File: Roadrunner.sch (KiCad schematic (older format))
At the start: 57 parts, among them J1 USB_OTG, J10 Digital, J11 ~WAKE, J13 SERIAL 4, J14 SERIAL 3, J15 -AREF, J16 +AREF, J17 SPI 2 (D22,D23), J19 SERIAL 2, J2 JTAG, J20 SPI 0, J21 SERIAL 1, J3 ~RST, J4 PF4, J5 ~HIB, J6 VIn, J7 Power, J8 Analog, J9 Digital, Q1 UM6K33N, Q2 UM6K33N, SW1 RESET, T1 M_Hole, T2 M_Hole, T3 M_Hole, T4 M_Hole, U1 TM4C123GH6PM, U2 LM1117-3.3, Y1 32.768Khz, Y2 16MHz

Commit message: Renaming project ro Roadrunner
Also include various routing changes and a new logo
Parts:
- C2: Description (none) -> 24pF ±5% 50V Ceramic Capacitor C0G, NP0 0603; Part # (none) -> CC0603JRNPO9BN240
- Q1, Q2: Part # (none) -> UM6K33NTN
- R1: Part # ERJ-3EKF1002V -> RC0603FR-0710KL
- R2: Part # ERJ-3EKF1004V -> RCG06031M00FKEA
- RN2: Part # YC164-JR-0710KL -> EXB-38V103JV
- U2: Part # (none) -> LM1117IMPX-3.3/NOPB
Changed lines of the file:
@@
 LIBS:tm4c123gh6pm
 LIBS:project_symbols
-LIBS:Arduino_Leo_Tiva-cache
+LIBS:Roadrunner-cache
 EELAYER 25 0
 EELAYER END
@@
 Title "Roadrunner (Arduino-Tiva)"
 Date "2017-07-22"
-Rev "v1.1"
+Rev "v1.1.2"
 Comp "Jacob Miller"
 Comment1 "TM4C123G"
@@
 F 1 "10k" V 1500 1050 50  0000 C CNN
 F 2 "Resistors_SMD:R_0603_HandSoldering" V 1430 1050 50  0001 C CNN
-F 3 "http://industrial.panasonic.com/www-cgi/jvcr13pz.cgi?E+PZ+3+AOA0002+ERJ3EKF1002V+7+WW" H 1500 1050 50  0001 C CNN
+F 3 "http://www.yageo.com/pdf/Pu-RC0603_51_PbFree_L_2.pdf" H 1500 1050 50  0001 C CNN
 F 4 "10k Ohm ±1% 0.1W, 1/10W Chip Resistor 0603 (1608 Metric) Automotive AEC-Q200 Thick Film" V 1500 1050 60  0001 C CNN "Description"
-F 5 "ERJ-3EKF1002V" V 1500 1050 60  0001 C CNN "Part #"
+F 5 "RC0603FR-0710KL" V 1500 1050 60  0001 C CNN "Part #"
 	1    1500 1050
 	1    0    0    -1
 $EndComp
 $Comp
-L +3.3V #PWR01
+L +3.3V #PWR6
 U 1 1 58E00512
 P 1500 800
-F 0 "#PWR01" H 1500 650 50  0001 C CNN
+F 0 "#PWR6" H 1500 650 50  0001 C CNN
 F 1 "+3.3V" H 1500 940 50  0000 C CNN
 F 2 "" H 1500 800 50  0001 C CNN
@@
 $EndComp
 $Comp
-L C_Small C2
-U 1 1 58E01071
-P 3450 4450
-F 0 "C2" H 3460 4520 50  0000 L CNN
-F 1 "24pF" H 3460 4370 50  0000 L CNN
-F 2 "Capacitors_SMD:C_0603" H 3450 4450 50  0001 C CNN
-F 3 "" H 3450 4450 50  0001 C CNN
-	1    3450 4450
-	0    -1   -1   0
-$EndComp
-$Comp
-L GNDREF #PWR02
+L GNDREF #PWR9
 U 1 1 58E01B5B
 P 3000 3700
-F 0 "#PWR02" H 3000 3450 50  0001 C CNN
+F 0 "#PWR9" H 3000 3450 50  0001 C CNN
 F 1 "GNDREF" H 3000 3550 50  0001 C CNN
 F 2 "" H 3000 3700 50  0001 C CNN
@@
 $EndComp
 $Comp
-L GNDREF #PWR03
+L GNDREF #PWR11
 U 1 1 58E01B81
 P 3500 3700
-F 0 "#PWR03" H 3500 3450 50  0001 C CNN
+F 0 "#PWR11" H 3500 3450 50  0001 C CNN
 F 1 "GNDREF" H 3500 3550 50  0001 C CNN
 F 2 "" H 3500 3700 50  0001 C CNN
@@
 $EndComp
 $Comp
-L GNDREF #PWR04
+L GNDREF #PWR2
 U 1 1 58E02126
 P 1000 1300
-F 0 "#PWR04" H 1000 1050 50  0001 C CNN
+F 0 "#PWR2" H 1000 1050 50  0001 C CNN
 F 1 "GNDREF" H 1000 1150 50  0001 C CNN
 F 2 "" H 1000 1300 50  0001 C CNN
@@
 $EndComp
 $Comp
-L GNDREF #PWR05
+L GNDREF #PWR1
 U 1 1 58E02513
 P 800 4950
-F 0 "#PWR05" H 800 4700 50  0001 C CNN
+F 0 "#PWR1" H 800 4700 50  0001 C CNN
 F 1 "GNDREF" H 800 4800 50  0001 C CNN
 F 2 "" H 800 4950 50  0001 C CNN
@@
 $EndComp
 $Comp
-L GNDREF #PWR06
+L GNDREF #PWR15
 U 1 1 58E0281C
 P 5550 5700
-F 0 "#PWR06" H 5550 5450 50  0001 C CNN
+F 0 "#PWR15" H 5550 5450 50  0001 C CNN
 F 1 "GNDREF" H 5550 5550 50  0001 C CNN
 F 2 "" H 5550 5700 50  0001 C CNN
@@
 $EndComp
 $Comp
-L +3.3V #PWR07
+L +3.3V #PWR16
 U 1 1 58E02E1C
 P 5650 900
-F 0 "#PWR07" H 5650 750 50  0001 C CNN
+F 0 "#PWR16" H 5650 750 50  0001 C CNN
 F 1 "+3.3V" H 5650 1040 50  0000 C CNN
 F 2 "" H 5650 900 50  0001 C CNN
@@
 F 1 "1M" V 1750 2000 50  0000 C CNN
 F 2 "Resistors_SMD:R_0603_HandSoldering" V 1680 2000 50  0001 C CNN
-F 3 "https://industrial.panasonic.com/cdbs/www-data/pdf/RDA0000/AOA0000C283.pdf" H 1750 2000 50  0001 C CNN
+F 3 "http://www.vishay.com/docs/20047/rcge3.pdf" H 1750 2000 50  0001 C CNN
 F 4 "1M Ohm ±1% 0.1W, 1/10W Chip Resistor 0603 (1608 Metric) Automotive AEC-Q200 Thick Film" V 1750 2000 60  0001 C CNN "Description"
-F 5 "ERJ-3EKF1004V" V 1750 2000 60  0001 C CNN "Part #"
+F 5 "RCG06031M00FKEA" V 1750 2000 60  0001 C CNN "Part #"
 	1    1750 2000
 	0    1    1    0
 $EndComp
 $Comp
-L +3.3V #PWR08
+L +3.3V #PWR8
 U 1 1 58E05812
 P 2000 1900
-F 0 "#PWR08" H 2000 1750 50  0001 C CNN
+F 0 "#PWR8" H 2000 1750 50  0001 C CNN
 F 1 "+3.3V" H 2000 2040 50  0000 C CNN
 F 2 "" H 2000 1900 50  0001 C CNN
@@
 $EndComp
 $Comp
-L +3.3V #PWR09
+L +3.3V #PWR14
 U 1 1 58E05E41
 P 5350 6200
-F 0 "#PWR09" H 5350 6050 50  0001 C CNN
+F 0 "#PWR14" H 5350 6050 50  0001 C CNN
 F 1 "+3.3V" H 5350 6340 50  0000 C CNN
 F 2 "" H 5350 6200 50  0001 C CNN
@@
 $EndComp
 $Comp
-L GNDREF #PWR010
+L GNDREF #PWR12
 U 1 1 58E09FA6
 P 4700 1150
-F 0 "#PWR010" H 4700 900 50  0001 C CNN
+F 0 "#PWR12" H 4700 900 50  0001 C CNN
 F 1 "GNDREF" H 4700 1000 50  0001 C CNN
 F 2 "" H 4700 1150 50  0001 C CNN
@@
 10(SS)
 $Comp
-L GNDREF #PWR011
+L GNDREF #PWR10
 U 1 1 58E19A27
 P 3350 6050
-F 0 "#PWR011" H 3350 5800 50  0001 C CNN
+F 0 "#PWR10" H 3350 5800 50  0001 C CNN
 F 1 "GNDREF" H 3350 5900 50  0001 C CNN
 F 2 "" H 3350 6050 50  0001 C CNN
@@
 $EndComp
 $Comp
-L GNDREF #PWR012
+L GNDREF #PWR5
 U 1 1 58E1A7DA
 P 1450 6600
-F 0 "#PWR012" H 1450 6350 50  0001 C CNN
+F 0 "#PWR5" H 1450 6350 50  0001 C CNN
 F 1 "GNDREF" H 1450 6450 50  0001 C CNN
 F 2 "" H 1450 6600 50  0001 C CNN
@@
 $EndComp
 $Comp
-L +3.3V #PWR013
+L +3.3V #PWR4
 U 1 1 58E1ADF7
 P 1350 5900
-F 0 "#PWR013" H 1350 5750 50  0001 C CNN
+F 0 "#PWR4" H 1350 5750 50  0001 C CNN
 F 1 "+3.3V" H 1350 6040 50  0000 C CNN
 F 2 "" H 1350 5900 50  0001 C CNN
@@
 $EndComp
 $Comp
-L +5V #PWR014
+L +5V #PWR3
 U 1 1 58E1AE4D
 P 1200 5750
-F 0 "#PWR014" H 1200 5600 50  0001 C CNN
+F 0 "#PWR3" H 1200 5600 50  0001 C CNN
 F 1 "+5V" H 1200 5890 50  0000 C CNN
 F 2 "" H 1200 5750 50  0001 C CNN
@@
 	5000 7250 5000 7300
 $Comp
-L +3.3V #PWR015
+L +3.3V #PWR17
 U 1 1 58E812E7
 P 5900 7200
-F 0 "#PWR015" H 5900 7050 50  0001 C CNN
+F 0 "#PWR17" H 5900 7050 50  0001 C CNN
 F 1 "+3.3V" H 5900 7340 50  0000 C CNN
 F 2 "" H 5900 7200 50  0001 C CNN
@@
 $EndComp
 $Comp
-L GNDREF #PWR016
+L GNDREF #PWR13
 U 1 1 58EEED9A
 P 4950 6850
-F 0 "#PWR016" H 4950 6600 50  0001 C CNN
+F 0 "#PWR13" H 4950 6600 50  0001 C CNN
 F 1 "GNDREF" H 4950 6700 50  0000 C CNN
 F 2 "" H 4950 6850 50  0001 C CNN
@@
 VDDC
 $Comp
-L GNDREF #PWR017
+L GNDREF #PWR18
 U 1 1 58E03A30
 P 5900 7600
-F 0 "#PWR017" H 5900 7350 50  0001 C CNN
+F 0 "#PWR18" H 5900 7350 50  0001 C CNN
 F 1 "GNDREF" H 5900 7450 50  0001 C CNN
 F 2 "" H 5900 7600 50  0001 C CNN
@@
 F 3 "http://www.ti.com/lit/ds/symlink/lm1117.pdf" H 4950 6350 50  0001 C CNN
 F 4 "Linear Voltage Regulator IC Positive Fixed Output 3.3V 800mA SOT-223-4" H 4950 6350 60  0001 C CNN "Description"
+F 5 "LM1117IMPX-3.3/NOPB" H 4950 6350 60  0001 C CNN "Part #"
 	1    4950 6350
 	1    0    0    -1
@@
 $EndComp
 $Comp
-L GNDREF #PWR018
+L GNDREF #PWR23
 U 1 1 5962AE49
 P 10700 3200
-F 0 "#PWR018" H 10700 2950 50  0001 C CNN
+F 0 "#PWR23" H 10700 2950 50  0001 C CNN
 F 1 "GNDREF" H 10700 3050 50  0001 C CNN
 F 2 "" H 10700 3200 50  0001 C CNN
@@
 $EndComp
 $Comp
-L GNDREF #PWR019
+L GNDREF #PWR19
 U 1 1 5962C255
 P 9800 3200
-F 0 "#PWR019" H 9800 2950 50  0001 C CNN
+F 0 "#PWR19" H 9800 2950 50  0001 C CNN
 F 1 "GNDREF" H 9800 3050 50  0001 C CNN
 F 2 "" H 9800 3200 50  0001 C CNN
@@
 F 2 "TO_SOT_Packages_SMD:SOT-363_SC-70-6_Handsoldering" H 10050 3275 50  0001 L CIN
 F 3 "http://www.rohm.com/web/global/datasheet/UM6K33N/um6k33n-e" H 10450 3600 50  0001 L CNN
+F 4 "UM6K33NTN" H 10250 3000 60  0001 C CNN "Part #"
 	1    10250 3000
 	1    0    0    -1
@@
 $EndComp
 $Comp
-L GNDREF #PWR020
+L GNDREF #PWR24
 U 1 1 59737761
 P 10700 4300
-F 0 "#PWR020" H 10700 4050 50  0001 C CNN
+F 0 "#PWR24" H 10700 4050 50  0001 C CNN
 F 1 "GNDREF" H 10700 4150 50  0001 C CNN
 F 2 "" H 10700 4300 50  0001 C CNN
@@
 $EndComp
 $Comp
-L GNDREF #PWR021
+L GNDREF #PWR20
 U 1 1 59737779
 P 9800 4300
-F 0 "#PWR021" H 9800 4050 50  0001 C CNN
+F 0 "#PWR20" H 9800 4050 50  0001 C CNN
 F 1 "GNDREF" H 9800 4150 50  0001 C CNN
 F 2 "" H 9800 4300 50  0001 C CNN
@@
 F 2 "TO_SOT_Packages_SMD:SOT-363_SC-70-6_Handsoldering" H 10050 4375 50  0001 L CIN
 F 3 "http://www.rohm.com/web/global/datasheet/UM6K33N/um6k33n-e" H 10450 4700 50  0001 L CNN
+F 4 "UM6K33NTN" H 10250 4100 60  0001 C CNN "Part #"
 	1    10250 4100
 	1    0    0    -1
@@
 F 1 "10k" V 10450 4950 50  0000 C CNN
 F 2 "Project-Symbols_Local:YC164-JR-0775RL" V 10525 4950 50  0001 C CNN
-F 3 "http://www.vishay.com/docs/31003/cra12es.pdf" H 10250 4950 50  0001 C CNN
-F 4 "YC164-JR-0710KL" V 10250 4950 60  0001 C CNN "Part #"
+F 3 "https://media.digikey.com/pdf/Data%20Sheets/Panasonic%20Resistors%20Thermistors%20PDFs/EXB38V%20Spec.pdf" H 10250 4950 50  0001 C CNN
+F 4 "EXB-38V103JV" V 10250 4950 60  0001 C CNN "Part #"
 F 5 "RES ARRAY 4 RES 10K OHM 1206" V 10250 4950 60  0001 C CNN "Description"
 	1    10250 4950
@@
 $EndComp
 $Comp
-L +3.3V #PWR022
+L +3.3V #PWR21
 U 1 1 59747BC5
 P 9950 1700
-F 0 "#PWR022" H 9950 1550 50  0001 C CNN
+F 0 "#PWR21" H 9950 1550 50  0001 C CNN
 F 1 "+3.3V" H 9950 1840 50  0000 C CNN
 F 2 "" H 9950 1700 50  0001 C CNN
@@
 PB6(MISO)
 $Comp
-L +3.3V #PWR023
+L +3.3V #PWR22
 U 1 1 5974C845
 P 10050 5050
-F 0 "#PWR023" H 10050 4900 50  0001 C CNN
+F 0 "#PWR22" H 10050 4900 50  0001 C CNN
 F 1 "+3.3V" H 10050 5190 50  0000 C CNN
 F 2 "" H 10050 5050 50  0001 C CNN
@@
 VBAT
 $Comp
-L +3.3V #PWR024
+L +3.3V #PWR7
 U 1 1 59753B9E
 P 1650 3300
-F 0 "#PWR024" H 1650 3150 50  0001 C CNN
+F 0 "#PWR7" H 1650 3150 50  0001 C CNN
 F 1 "+3.3V" H 1650 3440 50  0000 C CNN
 F 2 "" H 1650 3300 50  0001 C CNN
@@
 Wire Wire Line
 	1350 2850 1500 2850
+$Comp
+L C_Small C2
+U 1 1 597EDDE2
+P 3450 4450
+F 0 "C2" H 3460 4520 50  0000 L CNN
+F 1 "24pF" H 3460 4370 50  0000 L CNN
+F 2 "Capacitors_SMD:C_0603" H 3450 4450 50  0001 C CNN
+F 3 "http://www.yageo.com/documents/recent/UPY-GP_NP0_16V-to-50V_16.pdf" H 3450 4450 50  0001 C CNN
+F 4 "24pF ±5% 50V Ceramic Capacitor C0G, NP0 0603" H 3450 4450 60  0001 C CNN "Description"
+F 5 "CC0603JRNPO9BN240" H 3450 4450 60  0001 C CNN "Part #"
+	1    3450 4450
+	0    -1   -1   0
+$EndComp
 $EndSCHEMATC

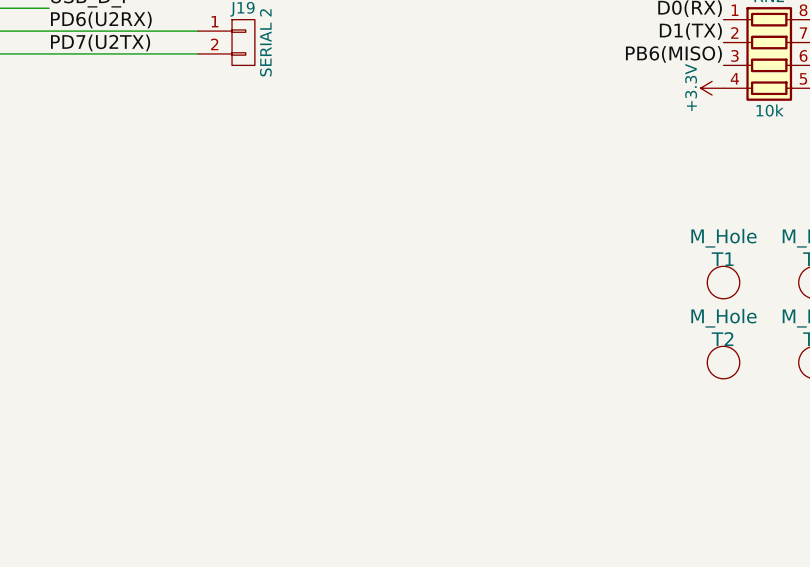
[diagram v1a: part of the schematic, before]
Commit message: Added additional 3.3V x4 and GND x4 headers to rear of board
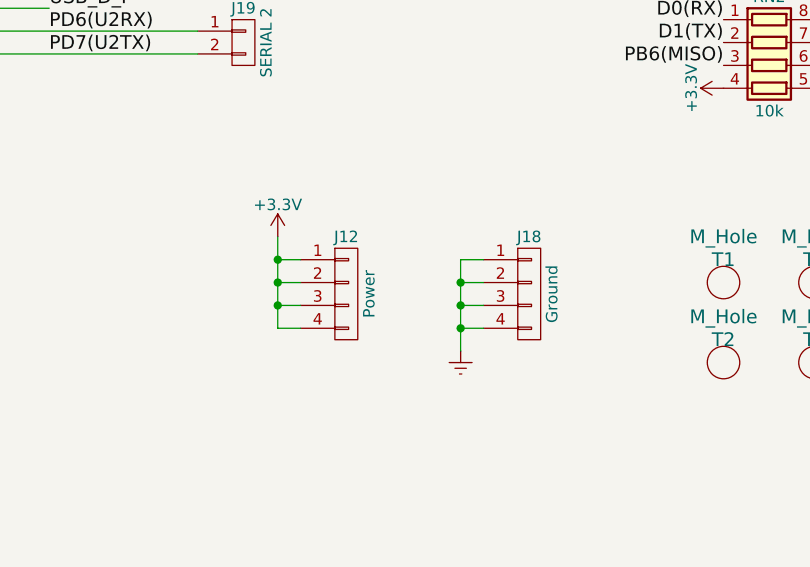
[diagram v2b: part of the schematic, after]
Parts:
- added J12: Power, Socket_Strips:Socket_Strip_Straight_1x04_Pitch2.54mm, symbol CONN_01X04
- added J18: Ground, Socket_Strips:Socket_Strip_Straight_1x04_Pitch2.54mm, symbol CONN_01X04
- D2, D3, D4, D5: footprint LEDs:LED_0805_HandSoldering -> LEDs:LED_0805
- Q1, Q2: footprint TO_SOT_Packages_SMD:SOT-363_SC-70-6_Handsoldering -> TO_SOT_Packages_SMD:SOT-363_SC-70-6
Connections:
- wire segments 199 -> 209
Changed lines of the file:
@@
 encoding utf-8
 Sheet 1 1
-Title "Roadrunner (Arduino-Tiva)"
-Date "2017-07-22"
+Title "Roadrunner"
+Date "2017-08-14"
 Rev "v1.1.2"
 Comp "Jacob Miller"
-Comment1 "TM4C123G"
+Comment1 "Arduino compatible board based on TI's TM4C123G"
 Comment2 ""
 Comment3 ""
@@
 $EndComp
 $Comp
-L +3.3V #PWR6
+L +3.3V #PWR01
 U 1 1 58E00512
 P 1500 800
-F 0 "#PWR6" H 1500 650 50  0001 C CNN
+F 0 "#PWR01" H 1500 650 50  0001 C CNN
 F 1 "+3.3V" H 1500 940 50  0000 C CNN
 F 2 "" H 1500 800 50  0001 C CNN
@@
 $EndComp
 $Comp
-L GNDREF #PWR9
+L GNDREF #PWR02
 U 1 1 58E01B5B
 P 3000 3700
-F 0 "#PWR9" H 3000 3450 50  0001 C CNN
+F 0 "#PWR02" H 3000 3450 50  0001 C CNN
 F 1 "GNDREF" H 3000 3550 50  0001 C CNN
 F 2 "" H 3000 3700 50  0001 C CNN
@@
 $EndComp
 $Comp
-L GNDREF #PWR11
+L GNDREF #PWR03
 U 1 1 58E01B81
 P 3500 3700
-F 0 "#PWR11" H 3500 3450 50  0001 C CNN
+F 0 "#PWR03" H 3500 3450 50  0001 C CNN
 F 1 "GNDREF" H 3500 3550 50  0001 C CNN
 F 2 "" H 3500 3700 50  0001 C CNN
@@
 $EndComp
 $Comp
-L GNDREF #PWR2
+L GNDREF #PWR04
 U 1 1 58E02126
 P 1000 1300
-F 0 "#PWR2" H 1000 1050 50  0001 C CNN
+F 0 "#PWR04" H 1000 1050 50  0001 C CNN
 F 1 "GNDREF" H 1000 1150 50  0001 C CNN
 F 2 "" H 1000 1300 50  0001 C CNN
@@
 $EndComp
 $Comp
-L GNDREF #PWR1
+L GNDREF #PWR05
 U 1 1 58E02513
 P 800 4950
-F 0 "#PWR1" H 800 4700 50  0001 C CNN
+F 0 "#PWR05" H 800 4700 50  0001 C CNN
 F 1 "GNDREF" H 800 4800 50  0001 C CNN
 F 2 "" H 800 4950 50  0001 C CNN
@@
 $EndComp
 $Comp
-L GNDREF #PWR15
+L GNDREF #PWR06
 U 1 1 58E0281C
 P 5550 5700
-F 0 "#PWR15" H 5550 5450 50  0001 C CNN
+F 0 "#PWR06" H 5550 5450 50  0001 C CNN
 F 1 "GNDREF" H 5550 5550 50  0001 C CNN
 F 2 "" H 5550 5700 50  0001 C CNN
@@
 $EndComp
 $Comp
-L +3.3V #PWR16
+L +3.3V #PWR07
 U 1 1 58E02E1C
 P 5650 900
-F 0 "#PWR16" H 5650 750 50  0001 C CNN
+F 0 "#PWR07" H 5650 750 50  0001 C CNN
 F 1 "+3.3V" H 5650 1040 50  0000 C CNN
 F 2 "" H 5650 900 50  0001 C CNN
@@
 $EndComp
 $Comp
-L +3.3V #PWR8
+L +3.3V #PWR08
 U 1 1 58E05812
 P 2000 1900
-F 0 "#PWR8" H 2000 1750 50  0001 C CNN
+F 0 "#PWR08" H 2000 1750 50  0001 C CNN
 F 1 "+3.3V" H 2000 2040 50  0000 C CNN
 F 2 "" H 2000 1900 50  0001 C CNN
@@
 $EndComp
 $Comp
-L +3.3V #PWR14
+L +3.3V #PWR09
 U 1 1 58E05E41
 P 5350 6200
-F 0 "#PWR14" H 5350 6050 50  0001 C CNN
+F 0 "#PWR09" H 5350 6050 50  0001 C CNN
 F 1 "+3.3V" H 5350 6340 50  0000 C CNN
 F 2 "" H 5350 6200 50  0001 C CNN
@@
 $EndComp
 $Comp
-L GNDREF #PWR12
+L GNDREF #PWR010
 U 1 1 58E09FA6
 P 4700 1150
-F 0 "#PWR12" H 4700 900 50  0001 C CNN
+F 0 "#PWR010" H 4700 900 50  0001 C CNN
 F 1 "GNDREF" H 4700 1000 50  0001 C CNN
 F 2 "" H 4700 1150 50  0001 C CNN
@@
 10(SS)
 $Comp
-L GNDREF #PWR10
+L GNDREF #PWR011
 U 1 1 58E19A27
 P 3350 6050
-F 0 "#PWR10" H 3350 5800 50  0001 C CNN
+F 0 "#PWR011" H 3350 5800 50  0001 C CNN
 F 1 "GNDREF" H 3350 5900 50  0001 C CNN
 F 2 "" H 3350 6050 50  0001 C CNN
@@
 $EndComp
 $Comp
-L GNDREF #PWR5
+L GNDREF #PWR012
 U 1 1 58E1A7DA
 P 1450 6600
-F 0 "#PWR5" H 1450 6350 50  0001 C CNN
+F 0 "#PWR012" H 1450 6350 50  0001 C CNN
 F 1 "GNDREF" H 1450 6450 50  0001 C CNN
 F 2 "" H 1450 6600 50  0001 C CNN
@@
 $EndComp
 $Comp
-L +3.3V #PWR4
+L +3.3V #PWR013
 U 1 1 58E1ADF7
 P 1350 5900
-F 0 "#PWR4" H 1350 5750 50  0001 C CNN
+F 0 "#PWR013" H 1350 5750 50  0001 C CNN
 F 1 "+3.3V" H 1350 6040 50  0000 C CNN
 F 2 "" H 1350 5900 50  0001 C CNN
@@
 $EndComp
 $Comp
-L +5V #PWR3
+L +5V #PWR014
 U 1 1 58E1AE4D
 P 1200 5750
-F 0 "#PWR3" H 1200 5600 50  0001 C CNN
+F 0 "#PWR014" H 1200 5600 50  0001 C CNN
 F 1 "+5V" H 1200 5890 50  0000 C CNN
 F 2 "" H 1200 5750 50  0001 C CNN
@@
 	5000 7250 5000 7300
 $Comp
-L +3.3V #PWR17
+L +3.3V #PWR015
 U 1 1 58E812E7
 P 5900 7200
-F 0 "#PWR17" H 5900 7050 50  0001 C CNN
+F 0 "#PWR015" H 5900 7050 50  0001 C CNN
 F 1 "+3.3V" H 5900 7340 50  0000 C CNN
 F 2 "" H 5900 7200 50  0001 C CNN
@@
 $EndComp
 $Comp
-L GNDREF #PWR13
+L GNDREF #PWR016
 U 1 1 58EEED9A
 P 4950 6850
-F 0 "#PWR13" H 4950 6600 50  0001 C CNN
+F 0 "#PWR016" H 4950 6600 50  0001 C CNN
 F 1 "GNDREF" H 4950 6700 50  0000 C CNN
 F 2 "" H 4950 6850 50  0001 C CNN
@@
 VDDC
 $Comp
-L GNDREF #PWR18
+L GNDREF #PWR017
 U 1 1 58E03A30
 P 5900 7600
-F 0 "#PWR18" H 5900 7350 50  0001 C CNN
+F 0 "#PWR017" H 5900 7350 50  0001 C CNN
 F 1 "GNDREF" H 5900 7450 50  0001 C CNN
 F 2 "" H 5900 7600 50  0001 C CNN
@@
 F 0 "D3" H 9700 2650 50  0000 C CNN
 F 1 "Green" H 9700 2450 50  0000 C CNN
-F 2 "LEDs:LED_0805_HandSoldering" H 9700 2550 50  0001 C CNN
+F 2 "LEDs:LED_0805" H 9700 2550 50  0001 C CNN
 F 3 "http://www.osram-os.com/Graphics/XPic9/00078860_0.pdf" H 9700 2550 50  0001 C CNN
 F 4 "20mA" H 9700 2550 60  0001 C CNN "Current "
@@
 $EndComp
 $Comp
-L GNDREF #PWR23
+L GNDREF #PWR018
 U 1 1 5962AE49
 P 10700 3200
-F 0 "#PWR23" H 10700 2950 50  0001 C CNN
+F 0 "#PWR018" H 10700 2950 50  0001 C CNN
 F 1 "GNDREF" H 10700 3050 50  0001 C CNN
 F 2 "" H 10700 3200 50  0001 C CNN
@@
 F 0 "D2" H 10800 2650 50  0000 C CNN
 F 1 "Green" H 10800 2450 50  0000 C CNN
-F 2 "LEDs:LED_0805_HandSoldering" H 10800 2550 50  0001 C CNN
+F 2 "LEDs:LED_0805" H 10800 2550 50  0001 C CNN
 F 3 "http://www.osram-os.com/Graphics/XPic9/00078860_0.pdf" H 10800 2550 50  0001 C CNN
 F 4 "20mA" H 10800 2550 60  0001 C CNN "Current "
@@
 $EndComp
 $Comp
-L GNDREF #PWR19
+L GNDREF #PWR019
 U 1 1 5962C255
 P 9800 3200
-F 0 "#PWR19" H 9800 2950 50  0001 C CNN
+F 0 "#PWR019" H 9800 2950 50  0001 C CNN
 F 1 "GNDREF" H 9800 3050 50  0001 C CNN
 F 2 "" H 9800 3200 50  0001 C CNN
@@
 F 0 "Q1" H 10050 3425 50  0000 L CNN
 F 1 "UM6K33N" H 10050 3350 50  0000 L CNN
-F 2 "TO_SOT_Packages_SMD:SOT-363_SC-70-6_Handsoldering" H 10050 3275 50  0001 L CIN
+F 2 "TO_SOT_Packages_SMD:SOT-363_SC-70-6" H 10050 3275 50  0001 L CIN
 F 3 "http://www.rohm.com/web/global/datasheet/UM6K33N/um6k33n-e" H 10450 3600 50  0001 L CNN
 F 4 "UM6K33NTN" H 10250 3000 60  0001 C CNN "Part #"
@@
 F 0 "D4" H 9700 3850 50  0000 C CNN
 F 1 "Green" H 9700 3650 50  0000 C CNN
-F 2 "LEDs:LED_0805_HandSoldering" H 9700 3750 50  0001 C CNN
+F 2 "LEDs:LED_0805" H 9700 3750 50  0001 C CNN
 F 3 "http://www.osram-os.com/Graphics/XPic9/00078860_0.pdf" H 9700 3750 50  0001 C CNN
 F 4 "20mA" H 9700 3750 60  0001 C CNN "Current "
@@
 $EndComp
 $Comp
-L GNDREF #PWR24
+L GNDREF #PWR020
 U 1 1 59737761
 P 10700 4300
-F 0 "#PWR24" H 10700 4050 50  0001 C CNN
+F 0 "#PWR020" H 10700 4050 50  0001 C CNN
 F 1 "GNDREF" H 10700 4150 50  0001 C CNN
 F 2 "" H 10700 4300 50  0001 C CNN
@@
 F 0 "D5" H 10800 3850 50  0000 C CNN
 F 1 "Green" H 10800 3650 50  0000 C CNN
-F 2 "LEDs:LED_0805_HandSoldering" H 10800 3750 50  0001 C CNN
+F 2 "LEDs:LED_0805" H 10800 3750 50  0001 C CNN
 F 3 "http://www.osram-os.com/Graphics/XPic9/00078860_0.pdf" H 10800 3750 50  0001 C CNN
 F 4 "20mA" H 10800 3750 60  0001 C CNN "Current "
@@
 $EndComp
 $Comp
-L GNDREF #PWR20
+L GNDREF #PWR021
 U 1 1 59737779
 P 9800 4300
-F 0 "#PWR20" H 9800 4050 50  0001 C CNN
+F 0 "#PWR021" H 9800 4050 50  0001 C CNN
 F 1 "GNDREF" H 9800 4150 50  0001 C CNN
 F 2 "" H 9800 4300 50  0001 C CNN
@@
 F 0 "Q2" H 10050 4525 50  0000 L CNN
 F 1 "UM6K33N" H 10050 4450 50  0000 L CNN
-F 2 "TO_SOT_Packages_SMD:SOT-363_SC-70-6_Handsoldering" H 10050 4375 50  0001 L CIN
+F 2 "TO_SOT_Packages_SMD:SOT-363_SC-70-6" H 10050 4375 50  0001 L CIN
 F 3 "http://www.rohm.com/web/global/datasheet/UM6K33N/um6k33n-e" H 10450 4700 50  0001 L CNN
 F 4 "UM6K33NTN" H 10250 4100 60  0001 C CNN "Part #"
@@
 $EndComp
 $Comp
-L +3.3V #PWR21
+L +3.3V #PWR022
 U 1 1 59747BC5
 P 9950 1700
-F 0 "#PWR21" H 9950 1550 50  0001 C CNN
+F 0 "#PWR022" H 9950 1550 50  0001 C CNN
 F 1 "+3.3V" H 9950 1840 50  0000 C CNN
 F 2 "" H 9950 1700 50  0001 C CNN
@@
 PB6(MISO)
 $Comp
-L +3.3V #PWR22
+L +3.3V #PWR023
 U 1 1 5974C845
 P 10050 5050
-F 0 "#PWR22" H 10050 4900 50  0001 C CNN
+F 0 "#PWR023" H 10050 4900 50  0001 C CNN
 F 1 "+3.3V" H 10050 5190 50  0000 C CNN
 F 2 "" H 10050 5050 50  0001 C CNN
@@
 VBAT
 $Comp
-L +3.3V #PWR7
+L +3.3V #PWR024
 U 1 1 59753B9E
 P 1650 3300
-F 0 "#PWR7" H 1650 3150 50  0001 C CNN
+F 0 "#PWR024" H 1650 3150 50  0001 C CNN
 F 1 "+3.3V" H 1650 3440 50  0000 C CNN
 F 2 "" H 1650 3300 50  0001 C CNN
@@
 	0    -1   -1   0
 $EndComp
+$Comp
+L CONN_01X04 J12
+U 1 1 599291D6
+P 8400 5950
+F 0 "J12" H 8400 6200 50  0000 C CNN
+F 1 "Power" V 8500 5950 50  0000 C CNN
+F 2 "Socket_Strips:Socket_Strip_Straight_1x04_Pitch2.54mm" H 8400 5950 50  0001 C CNN
+F 3 "" H 8400 5950 50  0001 C CNN
+	1    8400 5950
+	1    0    0    -1
+$EndComp
+$Comp
+L CONN_01X04 J18
+U 1 1 5992936E
+P 9200 5950
+F 0 "J18" H 9200 6200 50  0000 C CNN
+F 1 "Ground" V 9300 5950 50  0000 C CNN
+F 2 "Socket_Strips:Socket_Strip_Straight_1x04_Pitch2.54mm" H 9200 5950 50  0001 C CNN
+F 3 "" H 9200 5950 50  0001 C CNN
+	1    9200 5950
+	1    0    0    -1
+$EndComp
+$Comp
+L GNDREF #PWR025
+U 1 1 59929607
+P 8900 6200
+F 0 "#PWR025" H 8900 5950 50  0001 C CNN
+F 1 "GNDREF" H 8900 6050 50  0001 C CNN
+F 2 "" H 8900 6200 50  0001 C CNN
+F 3 "" H 8900 6200 50  0001 C CNN
+	1    8900 6200
+	1    0    0    -1
+$EndComp
+Wire Wire Line
+	8900 6200 8900 5800
+Wire Wire Line
+	8900 5800 9000 5800
+Wire Wire Line
+	9000 5900 8900 5900
+Connection ~ 8900 5900
+Wire Wire Line
+	9000 6000 8900 6000
+Connection ~ 8900 6000
+Wire Wire Line
+	9000 6100 8900 6100
+Connection ~ 8900 6100
+$Comp
+L +3.3V #PWR026
+U 1 1 5992A089
+P 8100 5700
+F 0 "#PWR026" H 8100 5550 50  0001 C CNN
+F 1 "+3.3V" H 8100 5840 50  0000 C CNN
+F 2 "" H 8100 5700 50  0001 C CNN
+F 3 "" H 8100 5700 50  0001 C CNN
+	1    8100 5700
+	1    0    0    -1
+$EndComp
+Wire Wire Line
+	8100 5700 8100 6100
+Wire Wire Line
+	8100 6100 8200 6100
+Wire Wire Line
+	8200 6000 8100 6000
+Connection ~ 8100 6000
+Wire Wire Line
+	8200 5900 8100 5900
+Connection ~ 8100 5900
+Wire Wire Line
+	8200 5800 8100 5800
+Connection ~ 8100 5800
 $EndSCHEMATC
